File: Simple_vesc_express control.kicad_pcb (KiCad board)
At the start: 2 copper layers, 48 x 38 mm, 45 parts, among them J1 Conn_01x04, J10 Conn_01x06, J2 Conn_01x04, J4 USB_C_Receptacle_USB2.0, J5 Conn_01x03, J6 Conn_01x03, J7 Conn_01x03, J8 Conn_01x02, J9 Conn_01x04, Q1 NMOS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

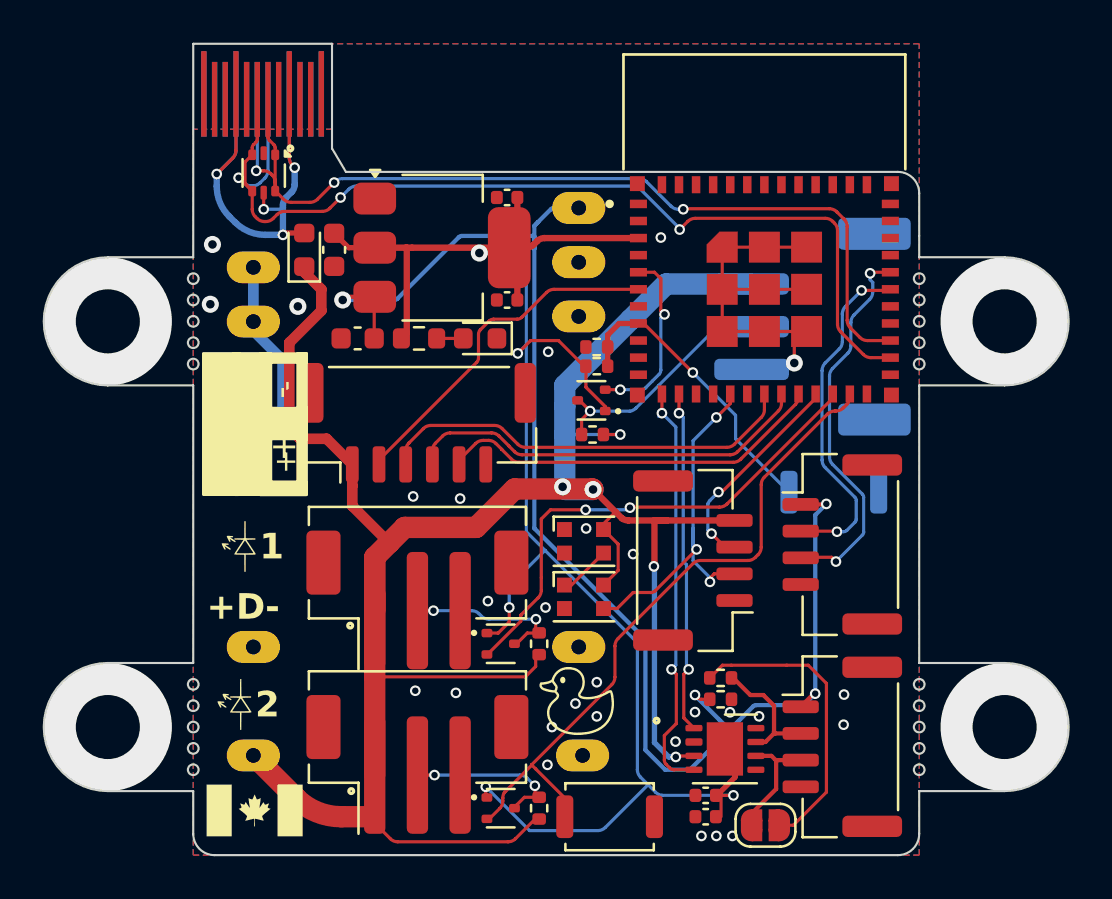
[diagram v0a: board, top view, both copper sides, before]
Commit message: changed usb powered parts
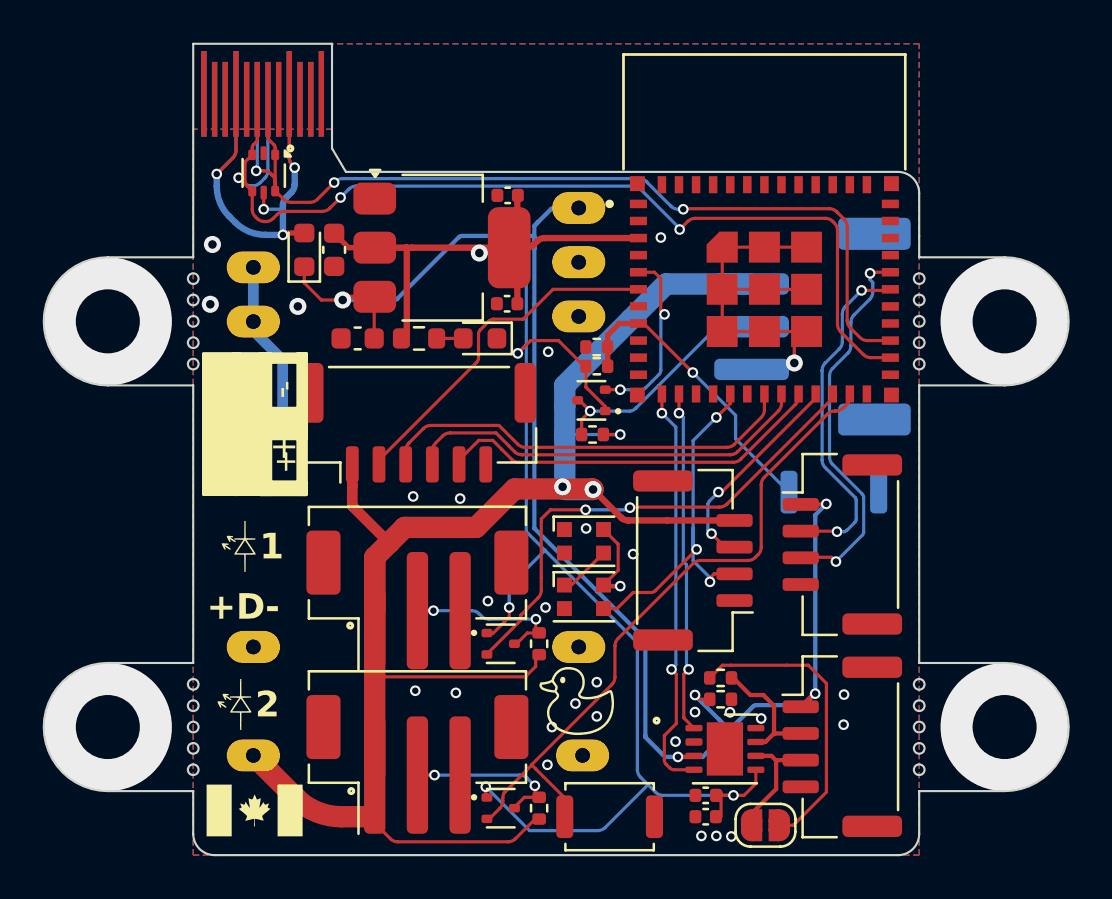
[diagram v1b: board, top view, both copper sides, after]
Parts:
- moved C10 0.17 mm to (114.7, 72.2)
- moved C11 0.10 mm to (114.7, 67.1)
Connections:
- D1 pad 1: +5V -> en
- D3 pad 4: +5V -> en
- D4 pad 4: +5V -> en
- U2 pad 3: +5V -> en
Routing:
- net +5V: track 109.8 -> 80.3 mm, vias 5 -> 3
- net en: track 68.6 -> 76.8 mm, vias 4 -> 6
